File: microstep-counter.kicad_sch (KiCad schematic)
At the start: 24 parts, among them U41 74HCT00, U42 74LS161, U43 74HCT138

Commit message: redid the eeprom
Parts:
- renumbered D73 to D72, D74 to D73, D75 to D74, D82 to D75, D83 to D76, D79 to D77, D77 to D79, D76 to D80, R119 to R116, R120 to R117, R121 to R118, R128 to R119, R129 to R120, R125 to R121, R124 to R122, R122 to R124, U43 to U44, U42 to U45

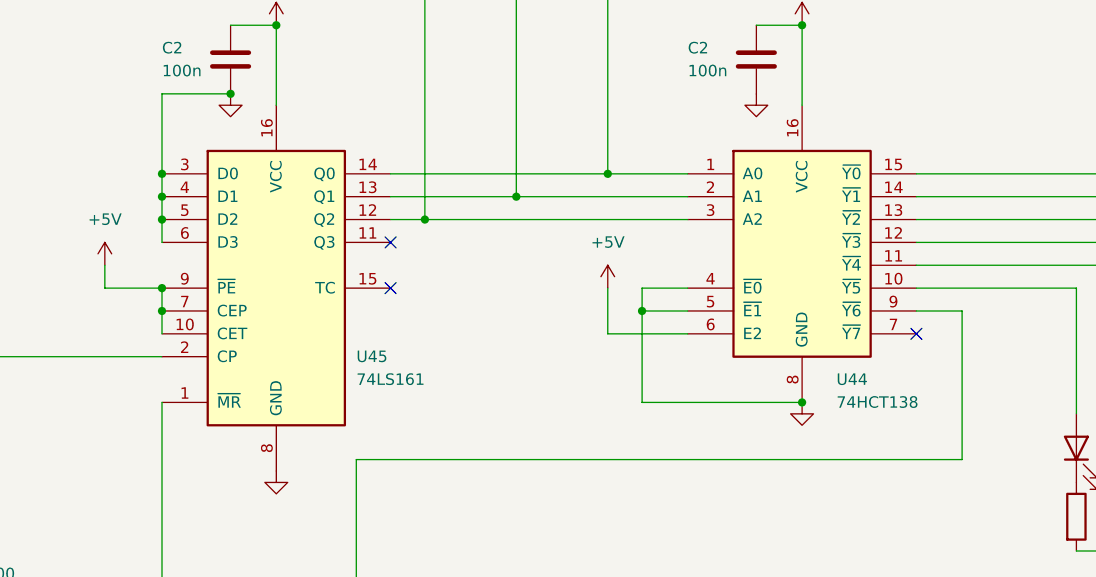
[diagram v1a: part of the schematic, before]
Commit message: changed symbols
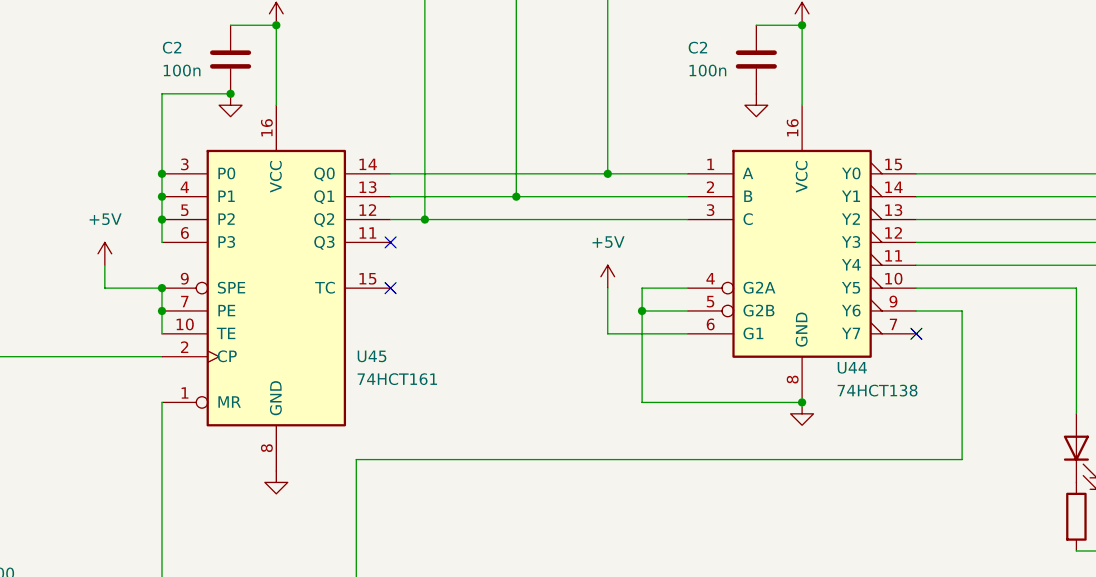
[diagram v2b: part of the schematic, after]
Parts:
- U44: symbol 74xx:74HCT138 -> 01_my_library:74HCT138
- U45: value 74LS161 -> 74HCT161; symbol 74xx:74LS161 -> 01_my_library:74HCT161
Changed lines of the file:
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@@
     )
   )
-  (symbol (lib_id "74xx:74LS161") (at 109.22 99.06 0) (unit 1)
+  (symbol (lib_id "01_my_library:74HCT161") (at 109.22 99.06 0) (unit 1)
     (in_bom yes) (on_board yes) (dnp no)
     (property "Reference" "U45" (at 118.11 106.68 0)
       (effects (font (size 1.27 1.27)) (justify left))
     )
-    (property "Value" "74LS161" (at 118.11 109.22 0)
+    (property "Value" "74HCT161" (at 118.11 109.22 0)
       (effects (font (size 1.27 1.27)) (justify left))
     )
@@
       (effects (font (size 1.27 1.27)) hide)
     )
-    (property "Datasheet" "http://www.ti.com/lit/gpn/sn74LS161" (at 109.22 99.06 0)
+    (property "Datasheet" "https://www.ti.com/lit/ds/symlink/cd54hct163.pdf?HQS=dis-mous-null-mousermode-dsf-pf-null-wwe&ts=1702794645288&ref_url=https%253A%252F%252Fwww.mouser.be%252F" (at 109.22 124.46 0)
       (effects (font (size 1.27 1.27)) hide)
     )
@@
     )
   )
-  (symbol (lib_id "74xx:74HCT138") (at 167.64 96.52 0) (unit 1)
-    (in_bom yes) (on_board yes) (dnp no)
-    (property "Reference" "U44" (at 171.45 109.22 0)
-      (effects (font (size 1.27 1.27)) (justify left))
-    )
-    (property "Value" "74HCT138" (at 171.45 111.76 0)
-      (effects (font (size 1.27 1.27)) (justify left))
-    )
-    (property "Footprint" "" (at 167.64 96.52 0)
-      (effects (font (size 1.27 1.27)) hide)
-    )
-    (property "Datasheet" "http://www.ti.com/lit/ds/symlink/cd74hc238.pdf" (at 167.64 96.52 0)
-      (effects (font (size 1.27 1.27)) hide)
-    )
+  (symbol (lib_id "01_my_library:74HCT138") (at 167.64 95.25 0) (unit 1)
+    (in_bom yes) (on_board yes) (dnp no)
+    (property "Reference" "U44" (at 171.45 107.95 0)
+      (effects (font (size 1.27 1.27)) (justify left))
+    )
+    (property "Value" "74HCT138" (at 171.45 110.49 0)
+      (effects (font (size 1.27 1.27)) (justify left))
+    )
+    (property "Footprint" "" (at 167.64 95.25 0)
+      (effects (font (size 1.27 1.27)) hide)
+    )
+    (property "Datasheet" "https://www.ti.com/lit/ds/symlink/sn54hct138.pdf?ts=1702793331407&ref_url=https%253A%252F%252Fwww.google.com%252F" (at 167.64 111.76 0)
+      (effects (font (size 1.27 1.27)) hide)
+    )

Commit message: some cleanup
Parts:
- renumbered D72 to D73, D73 to D74, D74 to D75, D75 to D76, D76 to D77, D77 to D78, D78 to D79, D79 to D80, D80 to D81, R116 to R117, R117 to R118, R118 to R119, R119 to R120, R120 to R121, R121 to R122, R122 to R123, R123 to R124, R124 to R125, U44 to U42, U45 to U43

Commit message: add arduino headers for programming
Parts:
- D73, D74, D75, D76, D77, D78, D79, D80, D81: footprint (none) -> LED_THT:LED_D5.0mm
- R117, R118, R119, R120, R121, R122, R123, R124, R125: footprint (none) -> Resistor_THT:R_Axial_DIN0204_L3.6mm_D1.6mm_P7.62mm_Horizontal
- U41: footprint (none) -> Package_DIP:DIP-14_W7.62mm
- U42, U43: footprint (none) -> Package_DIP:DIP-16_W7.62mm
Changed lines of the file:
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@@
       (effects (font (size 1.27 1.27)) (justify right))
     )
-    (property "Footprint" "" (at 223.52 116.84 0)
+    (property "Footprint" "LED_THT:LED_D5.0mm" (at 223.52 116.84 0)
       (effects (font (size 1.27 1.27)) hide)
     )
@@
       (effects (font (size 1.27 1.27)) (justify right))
     )
-    (property "Footprint" "" (at 236.22 116.84 0)
+    (property "Footprint" "LED_THT:LED_D5.0mm" (at 236.22 116.84 0)
       (effects (font (size 1.27 1.27)) hide)
     )
@@
       (effects (font (size 1.27 1.27)) (justify left))
     )
-    (property "Footprint" "" (at 221.742 124.46 90)
+    (property "Footprint" "Resistor_THT:R_Axial_DIN0204_L3.6mm_D1.6mm_P7.62mm_Horizontal" (at 221.742 124.46 90)
       (effects (font (size 1.27 1.27)) hide)
     )
@@
       (effects (font (size 1.27 1.27)) (justify left))
     )
-    (property "Footprint" "" (at 109.22 99.06 0)
+    (property "Footprint" "Package_DIP:DIP-16_W7.62mm" (at 109.22 99.06 0)
       (effects (font (size 1.27 1.27)) hide)
     )
@@
       (effects (font (size 1.27 1.27)) (justify right))
     )
-    (property "Footprint" "" (at 248.92 116.84 0)
+    (property "Footprint" "LED_THT:LED_D5.0mm" (at 248.92 116.84 0)
       (effects (font (size 1.27 1.27)) hide)
     )
@@
       (effects (font (size 1.27 1.27)) (justify left))
     )
-    (property "Footprint" "" (at 247.142 124.46 90)
+    (property "Footprint" "Resistor_THT:R_Axial_DIN0204_L3.6mm_D1.6mm_P7.62mm_Horizontal" (at 247.142 124.46 90)
       (effects (font (size 1.27 1.27)) hide)
     )
@@
       (effects (font (size 1.27 1.27)))
     )
-    (property "Footprint" "" (at 76.2 137.16 0)
+    (property "Footprint" "Package_DIP:DIP-14_W7.62mm" (at 76.2 137.16 0)
       (effects (font (size 1.27 1.27)) hide)
     )
@@
       (effects (font (size 1.27 1.27)) (justify left))
     )
-    (property "Footprint" "" (at 135.89 50.8 0)
+    (property "Footprint" "LED_THT:LED_D5.0mm" (at 135.89 50.8 0)
       (effects (font (size 1.27 1.27)) hide)
     )
@@
       (effects (font (size 1.27 1.27)) (justify right))
     )
-    (property "Footprint" "" (at 210.82 116.84 0)
+    (property "Footprint" "LED_THT:LED_D5.0mm" (at 210.82 116.84 0)
       (effects (font (size 1.27 1.27)) hide)
     )
@@
       (effects (font (size 1.27 1.27)) (justify left))
     )
-    (property "Footprint" "" (at 146.05 50.8 0)
+    (property "Footprint" "LED_THT:LED_D5.0mm" (at 146.05 50.8 0)
       (effects (font (size 1.27 1.27)) hide)
     )
@@
       (effects (font (size 1.27 1.27)) (justify left))
     )
-    (property "Footprint" "" (at 196.342 124.46 90)
+    (property "Footprint" "Resistor_THT:R_Axial_DIN0204_L3.6mm_D1.6mm_P7.62mm_Horizontal" (at 196.342 124.46 90)
       (effects (font (size 1.27 1.27)) hide)
     )
@@
       (effects (font (size 1.27 1.27)) (justify left))
     )
-    (property "Footprint" "" (at 259.842 124.46 90)
+    (property "Footprint" "Resistor_THT:R_Axial_DIN0204_L3.6mm_D1.6mm_P7.62mm_Horizontal" (at 259.842 124.46 90)
       (effects (font (size 1.27 1.27)) hide)
     )
@@
       (effects (font (size 1.27 1.27)) (justify right))
     )
-    (property "Footprint" "" (at 198.12 116.84 0)
+    (property "Footprint" "LED_THT:LED_D5.0mm" (at 198.12 116.84 0)
       (effects (font (size 1.27 1.27)) hide)
     )
@@
       (effects (font (size 1.27 1.27)) (justify left))
     )
-    (property "Footprint" "" (at 209.042 124.46 90)
+    (property "Footprint" "Resistor_THT:R_Axial_DIN0204_L3.6mm_D1.6mm_P7.62mm_Horizontal" (at 209.042 124.46 90)
       (effects (font (size 1.27 1.27)) hide)
     )
@@
       (effects (font (size 1.27 1.27)))
     )
-    (property "Footprint" "" (at 48.26 137.16 0)
+    (property "Footprint" "Package_DIP:DIP-14_W7.62mm" (at 48.26 137.16 0)
       (effects (font (size 1.27 1.27)) hide)
     )
@@
       (effects (font (size 1.27 1.27)) (justify left))
     )
-    (property "Footprint" "" (at 144.272 43.18 90)
+    (property "Footprint" "Resistor_THT:R_Axial_DIN0204_L3.6mm_D1.6mm_P7.62mm_Horizontal" (at 144.272 43.18 90)
       (effects (font (size 1.27 1.27)) hide)
     )
@@
       (effects (font (size 1.27 1.27)) (justify left))
     )
-    (property "Footprint" "" (at 134.112 43.18 90)
+    (property "Footprint" "Resistor_THT:R_Axial_DIN0204_L3.6mm_D1.6mm_P7.62mm_Horizontal" (at 134.112 43.18 90)
       (effects (font (size 1.27 1.27)) hide)
     )
@@
       (effects (font (size 1.27 1.27)) (justify right))
     )
-    (property "Footprint" "" (at 261.62 116.84 0)
+    (property "Footprint" "LED_THT:LED_D5.0mm" (at 261.62 116.84 0)
       (effects (font (size 1.27 1.27)) hide)
     )
@@
       (effects (font (size 1.27 1.27)) (justify left))
     )
-    (property "Footprint" "" (at 167.64 95.25 0)
+    (property "Footprint" "Package_DIP:DIP-16_W7.62mm" (at 167.64 95.25 0)
       (effects (font (size 1.27 1.27)) hide)
     )
@@
       (effects (font (size 1.27 1.27)) (justify left))
     )
-    (property "Footprint" "" (at 125.73 50.8 0)
+    (property "Footprint" "LED_THT:LED_D5.0mm" (at 125.73 50.8 0)
       (effects (font (size 1.27 1.27)) hide)
     )
@@
       (effects (font (size 1.27 1.27)) (justify left))
     )
-    (property "Footprint" "" (at 123.952 43.18 90)
+    (property "Footprint" "Resistor_THT:R_Axial_DIN0204_L3.6mm_D1.6mm_P7.62mm_Horizontal" (at 123.952 43.18 90)
       (effects (font (size 1.27 1.27)) hide)
     )
@@
       (effects (font (size 1.27 1.27)) (justify left))
     )
-    (property "Footprint" "" (at 234.442 124.46 90)
+    (property "Footprint" "Resistor_THT:R_Axial_DIN0204_L3.6mm_D1.6mm_P7.62mm_Horizontal" (at 234.442 124.46 90)
       (effects (font (size 1.27 1.27)) hide)
     )
@@
       (effects (font (size 1.27 1.27)) (justify left))
     )
-    (property "Footprint" "" (at 262.89 38.1 0)
-      (effects (font (size 1.27 1.27)) hide)
-    )
+    (property "Footprint" "Package_DIP:DIP-14_W7.62mm" (at 262.89 38.1 0)
+      (effects (font (size 1.27 1.27)) hide)
+    )

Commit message: trying to solve issues
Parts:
- renumbered U42 to U44, U43 to U45

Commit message: cleanup
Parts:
- renumbered D73 to D72, D74 to D73, D75 to D74, D76 to D75, D77 to D76, D78 to D77, D79 to D78, D80 to D79, D81 to D80, R117 to R116, R118 to R117, R119 to R118, R120 to R119, R121 to R120, R122 to R121, R123 to R122, R124 to R123, R125 to R124
